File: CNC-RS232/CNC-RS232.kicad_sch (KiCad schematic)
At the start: 50 parts, among them J1 DIN-5_180degree, J2 DIN-5_180degree, J3 DIN-5_180degree, J4 DIN-5_180degree, J5 DIN-5_180degree, Q1 BC547, Q2 BC557, Q3 BC547, Q4 BC547, U1 L7805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

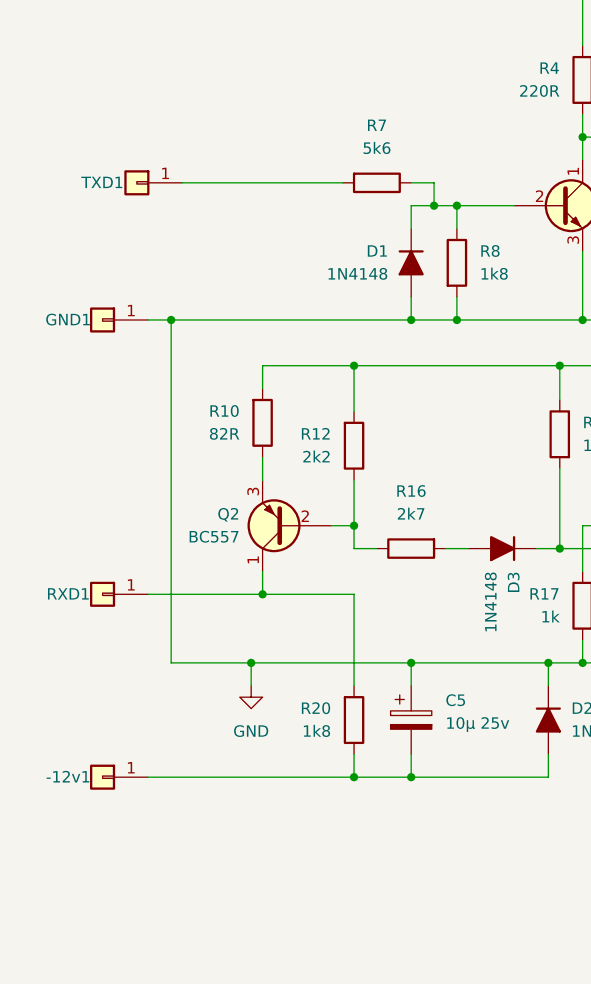
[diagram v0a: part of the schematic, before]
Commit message: fixed RS232 and Thru
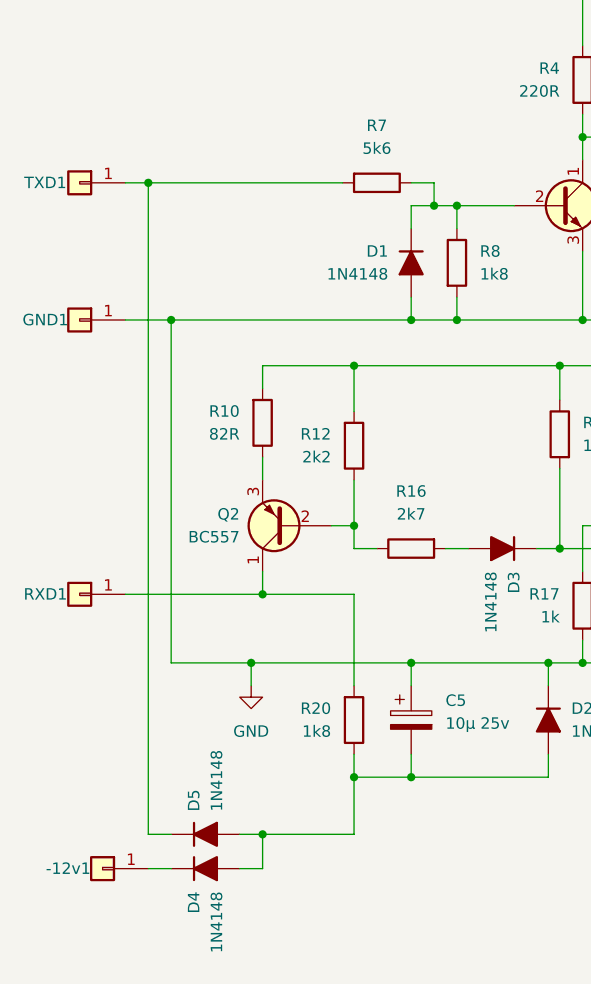
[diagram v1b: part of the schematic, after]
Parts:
- added D4, D5: 1N4148, Diode_THT:D_DO-35_SOD27_P10.16mm_Horizontal, symbol PCM_Diode_AKL:1N4148
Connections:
- net at C5.2, D2.2 (A), R20.1: now also D4.2 (A), D5.2 (A); no longer -12v1.1 (Pin_1)
- net at R7.2, TXD1.1 (Pin_1): now also D5.1 (K)
- new net: -12v1.1 (Pin_1), D4.1 (K)
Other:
- moved on the sheet: -12v1, GND1, RXD1, TXD1
